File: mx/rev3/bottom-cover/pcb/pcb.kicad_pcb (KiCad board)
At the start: 2 copper layers, 100 x 97.8 mm, 59 parts

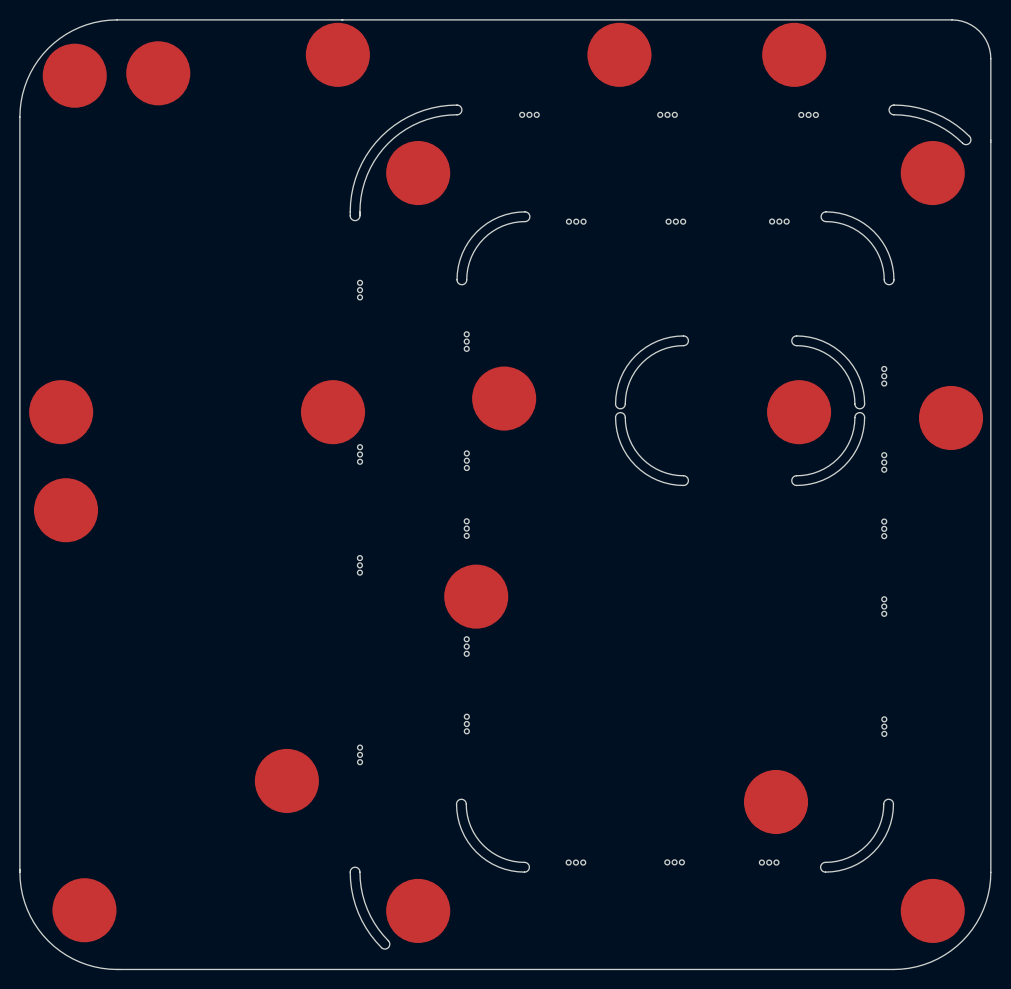
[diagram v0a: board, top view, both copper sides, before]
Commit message: M  giri-kicad-lib/switches_lib.pretty/Gateron_1.25u_v2.kicad_mod M  giri-kicad-lib/switches_lib.pretty/Gateron_1u_v2.kicad_mod M  giri-kicad-lib/switches_lib.pretty/Gateron_2u_v2.kicad_mod A  giri-kicad-lib/switches_lib.pretty/SMTSO_M2_FrontPad_M2_hole.kicad_mod A  giri-kicad-lib/switches_lib.pretty/Switch_Cutout2_MX.kicad_mod A  giri-kicad-lib/switches_lib.pretty/Switch_Cutout2_MX_1.25u.kicad_mod A  giri-kicad-lib/switches_lib.pretty/Switch_Cutout2_MX_2u.kicad_mod M  mx/rev3/bottom-cover/pcb/pcb.kicad_pcb M  mx/rev3/bottom-cover/pcb/pcb.kicad_prl M  mx/rev3/bottom-cover/pcb/pcb.kicad_sch M  mx/rev3/pcb-rev2/pcb/pcb.kicad_pcb M  mx/rev3/pcb-rev2/pcb/pcb.kicad_prl M  mx/rev3/pcb-rev2/pcb/pcb.kicad_sch M  mx/rev3/switch-plate-wide/fp-lib-table M  mx/rev3/switch-plate-wide/switch-plate-wide.kicad_pcb M  mx/rev3/switch-plate-wide/switch-plate-wide.kicad_sch A  mx/rev4/notes D  nrfStamp/rev1/pcb/~pcb.kicad_sch.lck D  rp2040stamp/rev2/pcb/~pcb.kicad_sch.lck M  rp2040stamp/rev3/pcb/fp-lib-table M  rp2040stamp/rev3/pcb/pcb.kicad_pcb M  rp2040stamp/rev3/pcb/pcb.kicad_prl M  rp2040stamp/rev3/pcb/pcb.kicad_sch M  rp2040stamp/rev3/pcb/sym-lib-table
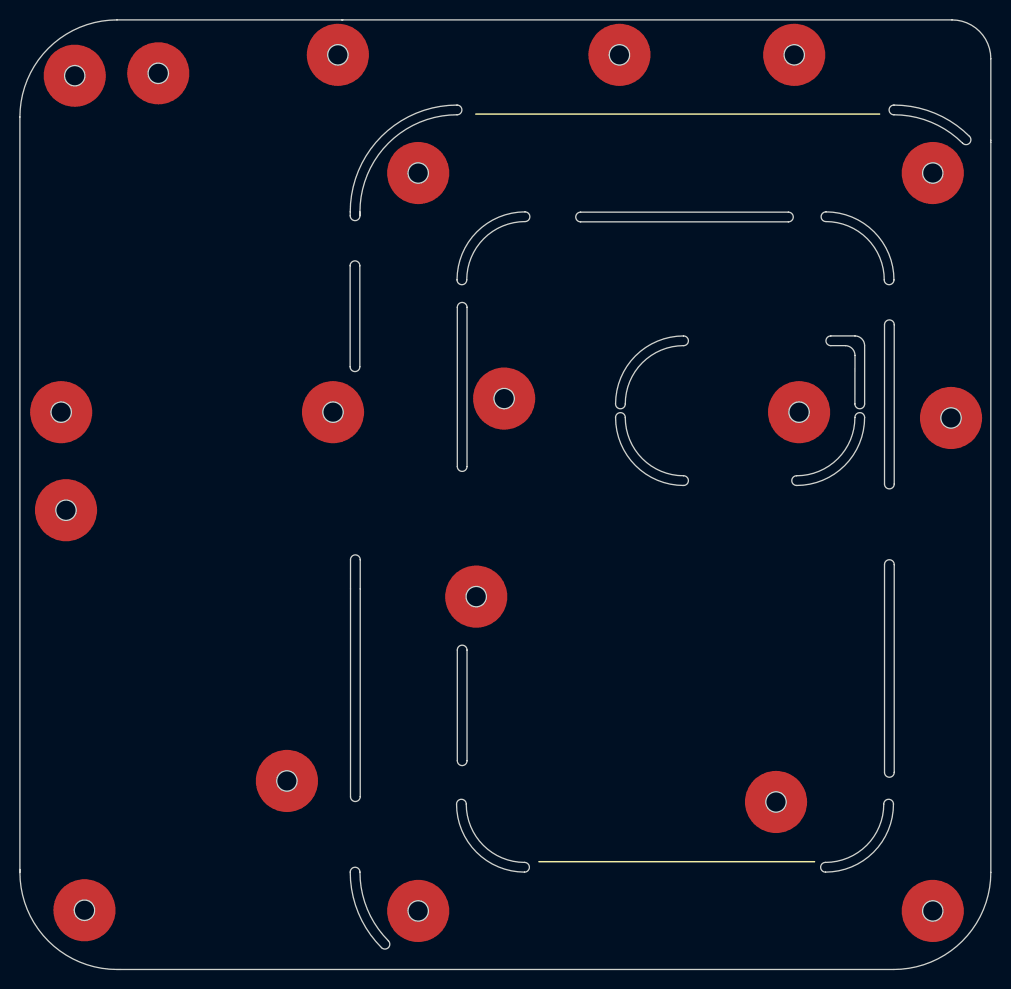
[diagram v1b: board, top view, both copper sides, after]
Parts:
- removed mouse-bite (x23): VAL**, giri:mouse-bite
- H1, H2, H3, H4, Hs1, Hs10, Hs11, Hs12, Hs13, Hs14, Hs15, Hs2, Hs3, Hs4, Hs5, Hs6, Hs7, Hs8, Hs9: footprint giri:SMTSO_M2_Front_Pad -> giri:SMTSO_M2_FrontPad_M2_hole
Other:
- outline, holes or cut-outs redrawn
